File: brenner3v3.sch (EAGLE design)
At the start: 14 parts, among them IC1 REG1117, Q2 BC328, Q3 BC328

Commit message: Added PCB
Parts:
- R5: device rcl:R-EU_0207/10 -> rcl:R-EU_0207/2V
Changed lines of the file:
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@@
 <setting verticaltext="up"/>
 </settings>
-<grid distance="100" unitdist="mil" unit="mil" style="lines" multiple="1" display="yes" altdistance="100" altunitdist="mil" altunit="mil"/>
+<grid distance="0.1" unitdist="inch" unit="inch" style="lines" multiple="1" display="no" altdistance="0.01" altunitdist="inch" altunit="inch"/>
 <layers>
-<layer number="1" name="Top" color="4" fill="1" visible="no" active="no"/>
-<layer number="16" name="Bottom" color="1" fill="1" visible="no" active="no"/>
-<layer number="17" name="Pads" color="2" fill="1" visible="no" active="no"/>
-<layer number="18" name="Vias" color="2" fill="1" visible="no" active="no"/>
-<layer number="19" name="Unrouted" color="6" fill="1" visible="no" active="no"/>
-<layer number="20" name="Dimension" color="15" fill="1" visible="no" active="no"/>
-<layer number="21" name="tPlace" color="7" fill="1" visible="no" active="no"/>
-<layer number="22" name="bPlace" color="7" fill="1" visible="no" active="no"/>
-<layer number="23" name="tOrigins" color="15" fill="1" visible="no" active="no"/>
-<layer number="24" name="bOrigins" color="15" fill="1" visible="no" active="no"/>
-<layer number="25" name="tNames" color="7" fill="1" visible="no" active="no"/>
-<layer number="26" name="bNames" color="7" fill="1" visible="no" active="no"/>
-<layer number="27" name="tValues" color="7" fill="1" visible="no" active="no"/>
-<layer number="28" name="bValues" color="7" fill="1" visible="no" active="no"/>
+<layer number="1" name="Top" color="4" fill="1" visible="yes" active="no"/>
+<layer number="16" name="Bottom" color="1" fill="1" visible="yes" active="no"/>
+<layer number="17" name="Pads" color="2" fill="1" visible="yes" active="no"/>
+<layer number="18" name="Vias" color="2" fill="1" visible="yes" active="no"/>
+<layer number="19" name="Unrouted" color="6" fill="1" visible="yes" active="no"/>
+<layer number="20" name="Dimension" color="15" fill="1" visible="yes" active="no"/>
+<layer number="21" name="tPlace" color="7" fill="1" visible="yes" active="no"/>
+<layer number="22" name="bPlace" color="7" fill="1" visible="yes" active="no"/>
+<layer number="23" name="tOrigins" color="15" fill="1" visible="yes" active="no"/>
+<layer number="24" name="bOrigins" color="15" fill="1" visible="yes" active="no"/>
+<layer number="25" name="tNames" color="7" fill="1" visible="yes" active="no"/>
+<layer number="26" name="bNames" color="7" fill="1" visible="yes" active="no"/>
+<layer number="27" name="tValues" color="7" fill="1" visible="yes" active="no"/>
+<layer number="28" name="bValues" color="7" fill="1" visible="yes" active="no"/>
 <layer number="29" name="tStop" color="7" fill="3" visible="no" active="no"/>
 <layer number="30" name="bStop" color="7" fill="6" visible="no" active="no"/>
@@
 <layer number="35" name="tGlue" color="7" fill="4" visible="no" active="no"/>
 <layer number="36" name="bGlue" color="7" fill="5" visible="no" active="no"/>
-<layer number="37" name="tTest" color="7" fill="1" visible="no" active="no"/>
-<layer number="38" name="bTest" color="7" fill="1" visible="no" active="no"/>
+<layer number="37" name="tTest" color="7" fill="1" visible="yes" active="no"/>
+<layer number="38" name="bTest" color="7" fill="1" visible="yes" active="no"/>
 <layer number="39" name="tKeepout" color="4" fill="11" visible="no" active="no"/>
 <layer number="40" name="bKeepout" color="1" fill="11" visible="no" active="no"/>
@@
 <layer number="44" name="Drills" color="7" fill="1" visible="no" active="no"/>
 <layer number="45" name="Holes" color="7" fill="1" visible="no" active="no"/>
-<layer number="46" name="Milling" color="3" fill="1" visible="no" active="no"/>
-<layer number="47" name="Measures" color="7" fill="1" visible="no" active="no"/>
-<layer number="48" name="Document" color="7" fill="1" visible="no" active="no"/>
-<layer number="49" name="Reference" color="7" fill="1" visible="no" active="no"/>
-<layer number="51" name="tDocu" color="7" fill="1" visible="no" active="no"/>
-<layer number="52" name="bDocu" color="7" fill="1" visible="no" active="no"/>
+<layer number="46" name="Milling" color="3" fill="1" visible="yes" active="no"/>
+<layer number="47" name="Measures" color="7" fill="1" visible="yes" active="no"/>
+<layer number="48" name="Document" color="7" fill="1" visible="yes" active="no"/>
+<layer number="49" name="Reference" color="7" fill="1" visible="yes" active="no"/>
+<layer number="51" name="tDocu" color="7" fill="1" visible="yes" active="no"/>
+<layer number="52" name="bDocu" color="7" fill="1" visible="yes" active="no"/>
 <layer number="91" name="Nets" color="2" fill="1" visible="yes" active="yes"/>
 <layer number="92" name="Busses" color="1" fill="1" visible="yes" active="yes"/>
@@
 <part name="R3" library="rcl" deviceset="R-EU_" device="0207/10" value="10"/>
 <part name="R4" library="rcl" deviceset="R-EU_" device="0207/10" value="10"/>
-<part name="R5" library="rcl" deviceset="R-EU_" device="0207/10" value="820"/>
+<part name="R5" library="rcl" deviceset="R-EU_" device="0207/2V" value="820"/>
 <part name="D1" library="diode" deviceset="1N4004" device=""/>
 <part name="Q2" library="transistor" deviceset="*-PNP-" device="TO92-EBC" technology="BC328-25" value="BC328"/>

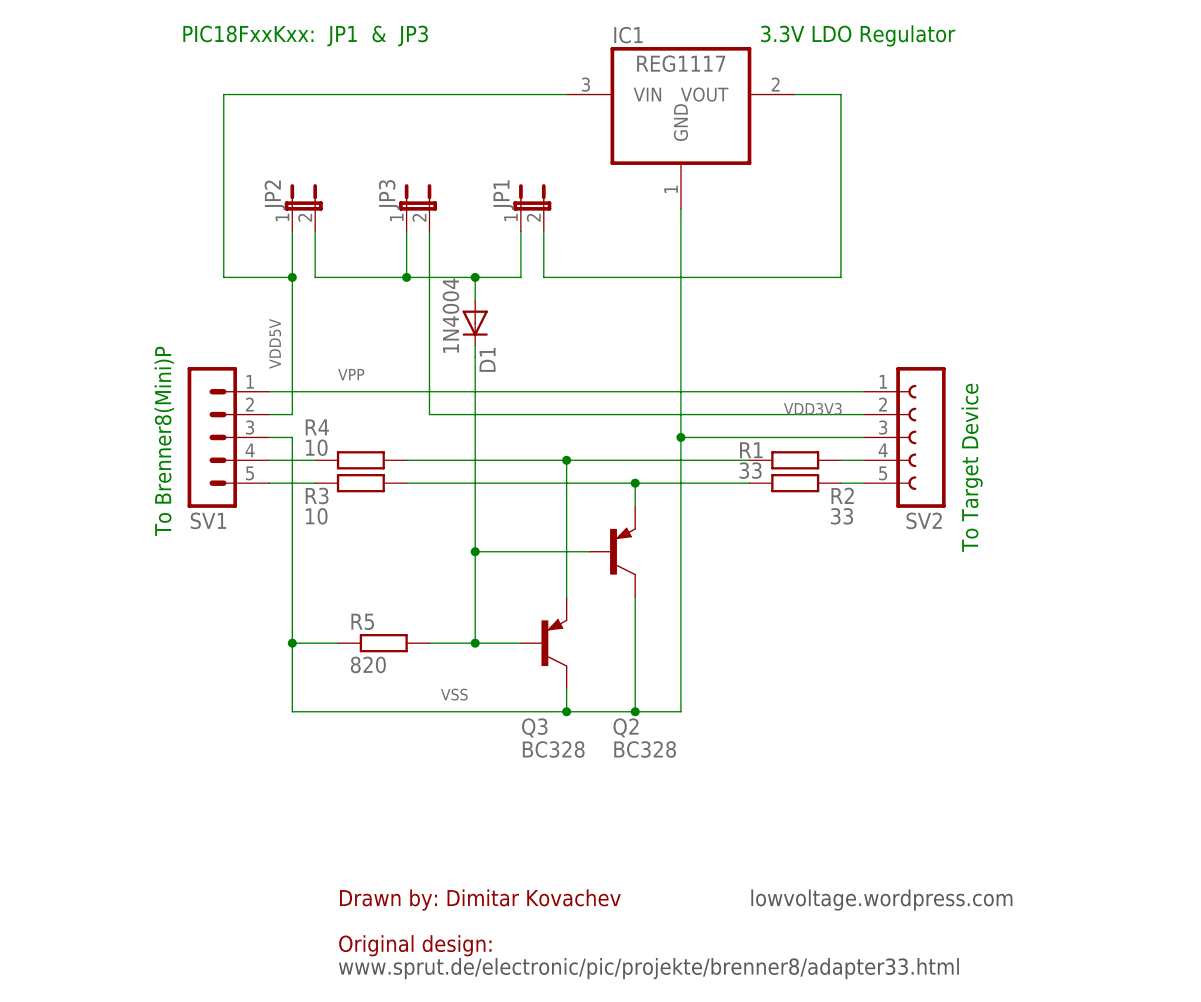
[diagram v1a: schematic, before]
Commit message: Simplified schematic & layout
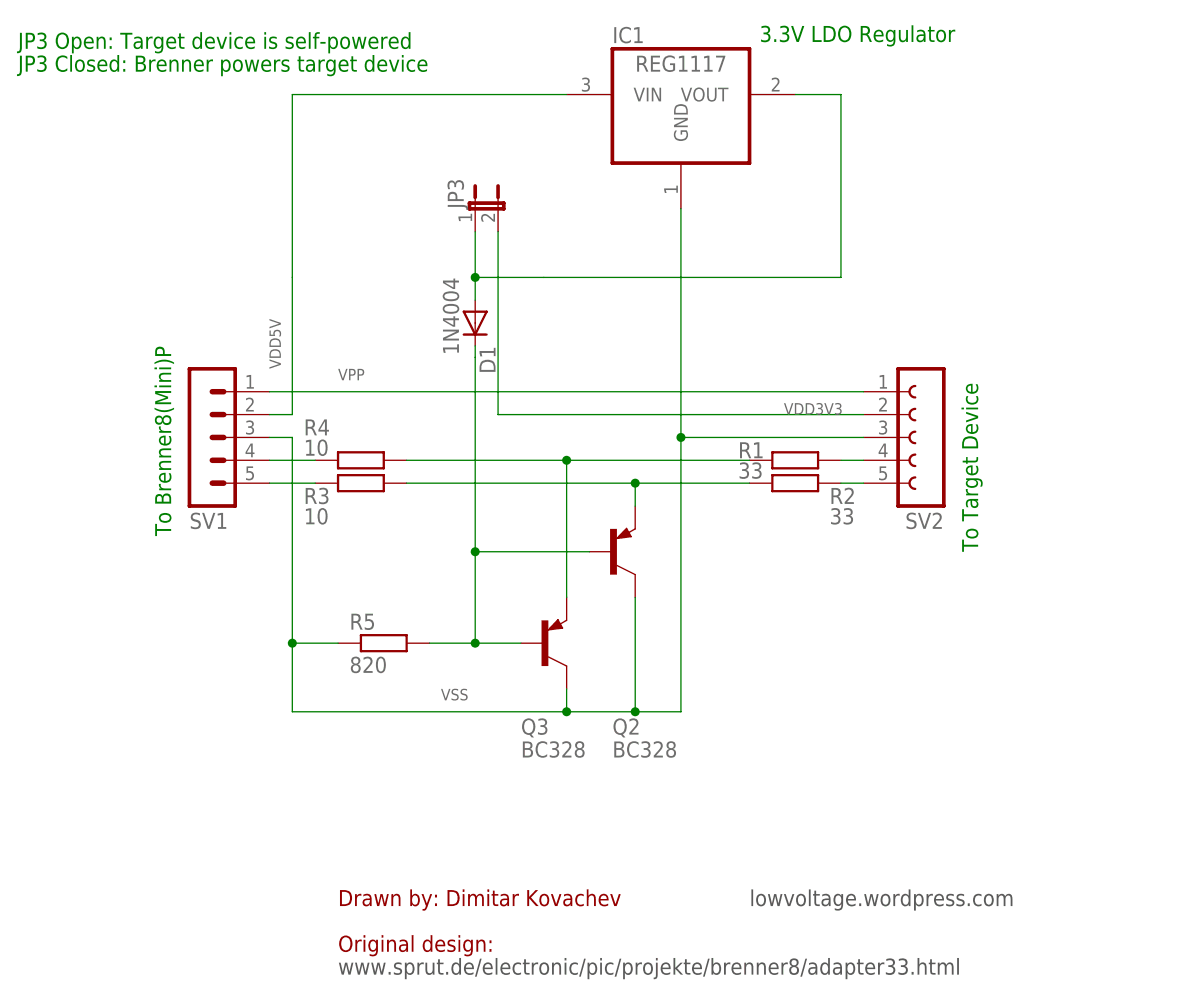
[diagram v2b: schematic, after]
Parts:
- removed JP1, JP2: (no value), jumper:JP1E
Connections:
- removed net N$1: IC1.VOUT, JP1.2
- net N$12: now also IC1.VOUT; no longer JP1.1, JP2.2
- net VDD5V: no longer JP2.1
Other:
- note added: "JP3 Closed: Brenner powers target device"
- note added: "JP3 Open: Target device is self-powered"
- note removed: "PIC18FxxKxx: JP1 & JP3"
- moved on the sheet: JP3
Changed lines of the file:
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@@
 <grid distance="0.1" unitdist="inch" unit="inch" style="lines" multiple="1" display="no" altdistance="0.01" altunitdist="inch" altunit="inch"/>
 <layers>
-<layer number="1" name="Top" color="4" fill="1" visible="yes" active="no"/>
-<layer number="16" name="Bottom" color="1" fill="1" visible="yes" active="no"/>
-<layer number="17" name="Pads" color="2" fill="1" visible="yes" active="no"/>
-<layer number="18" name="Vias" color="2" fill="1" visible="yes" active="no"/>
-<layer number="19" name="Unrouted" color="6" fill="1" visible="yes" active="no"/>
-<layer number="20" name="Dimension" color="15" fill="1" visible="yes" active="no"/>
-<layer number="21" name="tPlace" color="7" fill="1" visible="yes" active="no"/>
-<layer number="22" name="bPlace" color="7" fill="1" visible="yes" active="no"/>
-<layer number="23" name="tOrigins" color="15" fill="1" visible="yes" active="no"/>
-<layer number="24" name="bOrigins" color="15" fill="1" visible="yes" active="no"/>
-<layer number="25" name="tNames" color="7" fill="1" visible="yes" active="no"/>
-<layer number="26" name="bNames" color="7" fill="1" visible="yes" active="no"/>
-<layer number="27" name="tValues" color="7" fill="1" visible="yes" active="no"/>
-<layer number="28" name="bValues" color="7" fill="1" visible="yes" active="no"/>
+<layer number="1" name="Top" color="4" fill="1" visible="no" active="no"/>
+<layer number="16" name="Bottom" color="1" fill="1" visible="no" active="no"/>
+<layer number="17" name="Pads" color="2" fill="1" visible="no" active="no"/>
+<layer number="18" name="Vias" color="2" fill="1" visible="no" active="no"/>
+<layer number="19" name="Unrouted" color="6" fill="1" visible="no" active="no"/>
+<layer number="20" name="Dimension" color="15" fill="1" visible="no" active="no"/>
+<layer number="21" name="tPlace" color="7" fill="1" visible="no" active="no"/>
+<layer number="22" name="bPlace" color="7" fill="1" visible="no" active="no"/>
+<layer number="23" name="tOrigins" color="15" fill="1" visible="no" active="no"/>
+<layer number="24" name="bOrigins" color="15" fill="1" visible="no" active="no"/>
+<layer number="25" name="tNames" color="7" fill="1" visible="no" active="no"/>
+<layer number="26" name="bNames" color="7" fill="1" visible="no" active="no"/>
+<layer number="27" name="tValues" color="7" fill="1" visible="no" active="no"/>
+<layer number="28" name="bValues" color="7" fill="1" visible="no" active="no"/>
 <layer number="29" name="tStop" color="7" fill="3" visible="no" active="no"/>
 <layer number="30" name="bStop" color="7" fill="6" visible="no" active="no"/>
@@
 <layer number="35" name="tGlue" color="7" fill="4" visible="no" active="no"/>
 <layer number="36" name="bGlue" color="7" fill="5" visible="no" active="no"/>
-<layer number="37" name="tTest" color="7" fill="1" visible="yes" active="no"/>
-<layer number="38" name="bTest" color="7" fill="1" visible="yes" active="no"/>
+<layer number="37" name="tTest" color="7" fill="1" visible="no" active="no"/>
+<layer number="38" name="bTest" color="7" fill="1" visible="no" active="no"/>
 <layer number="39" name="tKeepout" color="4" fill="11" visible="no" active="no"/>
 <layer number="40" name="bKeepout" color="1" fill="11" visible="no" active="no"/>
@@
 <layer number="44" name="Drills" color="7" fill="1" visible="no" active="no"/>
 <layer number="45" name="Holes" color="7" fill="1" visible="no" active="no"/>
-<layer number="46" name="Milling" color="3" fill="1" visible="yes" active="no"/>
-<layer number="47" name="Measures" color="7" fill="1" visible="yes" active="no"/>
-<layer number="48" name="Document" color="7" fill="1" visible="yes" active="no"/>
-<layer number="49" name="Reference" color="7" fill="1" visible="yes" active="no"/>
-<layer number="51" name="tDocu" color="7" fill="1" visible="yes" active="no"/>
-<layer number="52" name="bDocu" color="7" fill="1" visible="yes" active="no"/>
+<layer number="46" name="Milling" color="3" fill="1" visible="no" active="no"/>
+<layer number="47" name="Measures" color="7" fill="1" visible="no" active="no"/>
+<layer number="48" name="Document" color="7" fill="1" visible="no" active="no"/>
+<layer number="49" name="Reference" color="7" fill="1" visible="no" active="no"/>
+<layer number="51" name="tDocu" color="7" fill="1" visible="no" active="no"/>
+<layer number="52" name="bDocu" color="7" fill="1" visible="no" active="no"/>
 <layer number="91" name="Nets" color="2" fill="1" visible="yes" active="yes"/>
 <layer number="92" name="Busses" color="1" fill="1" visible="yes" active="yes"/>
@@
 <part name="FRAME1" library="frames" deviceset="DINA4_P" device=""/>
 <part name="IC1" library="burr-brown" deviceset="REG1117" device=""/>
-<part name="JP1" library="jumper" deviceset="JP1E" device=""/>
-<part name="JP2" library="jumper" deviceset="JP1E" device=""/>
 <part name="JP3" library="jumper" deviceset="JP1E" device=""/>
 <part name="R1" library="rcl" deviceset="R-EU_" device="0207/10" value="33"/>
@@
 <text x="160.02" y="134.62" size="1.778" layer="91" rot="R180">3.3V LDO Regulator</text>
 <text x="71.12" y="99.06" size="1.778" layer="91" rot="R270">To Brenner8(Mini)P</text>
-<text x="101.6" y="134.62" size="1.778" layer="91" rot="R180">PIC18FxxKxx:  JP1  &amp;  JP3</text>
+<text x="55.88" y="132.08" size="1.778" layer="91">JP3 Open: Target device is self-powered</text>
+<text x="55.88" y="129.54" size="1.778" layer="91">JP3 Closed: Brenner powers target device</text>
 </plain>
 <instances>
@@
 <instance part="FRAME1" gate="G$2" x="88.9" y="5.08"/>
 <instance part="IC1" gate="G$1" x="129.54" y="127"/>
-<instance part="JP1" gate="A" x="111.76" y="114.3"/>
-<instance part="JP2" gate="A" x="86.36" y="114.3"/>
-<instance part="JP3" gate="A" x="99.06" y="114.3"/>
+<instance part="JP3" gate="A" x="106.68" y="114.3"/>
 <instance part="R1" gate="G$1" x="142.24" y="86.36" smashed="yes">
 <attribute name="NAME" x="135.89" y="86.5886" size="1.778" layer="95"/>
@@
 <segment>
 <pinref part="SV1" gate="G$1" pin="2"/>
-<pinref part="JP2" gate="A" pin="1"/>
 <wire x1="83.82" y1="91.44" x2="86.36" y2="91.44" width="0.1524" layer="91"/>
 <wire x1="86.36" y1="91.44" x2="86.36" y2="106.68" width="0.1524" layer="91"/>
-<wire x1="86.36" y1="106.68" x2="86.36" y2="111.76" width="0.1524" layer="91"/>
-<wire x1="86.36" y1="106.68" x2="78.74" y2="106.68" width="0.1524" layer="91"/>
-<wire x1="78.74" y1="106.68" x2="78.74" y2="127" width="0.1524" layer="91"/>
-<junction x="86.36" y="106.68"/>
+<wire x1="86.36" y1="106.68" x2="86.36" y2="127" width="0.1524" layer="91"/>
 <pinref part="IC1" gate="G$1" pin="VIN"/>
-<wire x1="78.74" y1="127" x2="116.84" y2="127" width="0.1524" layer="91"/>
+<wire x1="86.36" y1="127" x2="116.84" y2="127" width="0.1524" layer="91"/>
 <label x="85.09" y="96.52" size="1.27" layer="95" rot="R90"/>
 </segment>
 </net>
-<net name="N$1" class="0">
-<segment>
+<net name="N$12" class="0">
+<segment>
+<pinref part="JP3" gate="A" pin="1"/>
+<wire x1="106.68" y1="111.76" x2="106.68" y2="106.68" width="0.1524" layer="91"/>
+<pinref part="D1" gate="1" pin="A"/>
+<wire x1="106.68" y1="104.14" x2="106.68" y2="106.68" width="0.1524" layer="91"/>
+<junction x="106.68" y="106.68"/>
 <pinref part="IC1" gate="G$1" pin="VOUT"/>
 <wire x1="142.24" y1="127" x2="147.32" y2="127" width="0.1524" layer="91"/>
 <wire x1="147.32" y1="127" x2="147.32" y2="106.68" width="0.1524" layer="91"/>
 <wire x1="147.32" y1="106.68" x2="114.3" y2="106.68" width="0.1524" layer="91"/>
-<pinref part="JP1" gate="A" pin="2"/>
-<wire x1="114.3" y1="106.68" x2="114.3" y2="111.76" width="0.1524" layer="91"/>
-</segment>
-</net>
-<net name="N$12" class="0">
-<segment>
-<pinref part="JP2" gate="A" pin="2"/>
-<wire x1="88.9" y1="111.76" x2="88.9" y2="106.68" width="0.1524" layer="91"/>
-<wire x1="88.9" y1="106.68" x2="99.06" y2="106.68" width="0.1524" layer="91"/>
-<pinref part="JP1" gate="A" pin="1"/>
-<wire x1="99.06" y1="106.68" x2="106.68" y2="106.68" width="0.1524" layer="91"/>
-<wire x1="106.68" y1="106.68" x2="111.76" y2="106.68" width="0.1524" layer="91"/>
-<wire x1="111.76" y1="106.68" x2="111.76" y2="111.76" width="0.1524" layer="91"/>
-<pinref part="JP3" gate="A" pin="1"/>
-<wire x1="99.06" y1="111.76" x2="99.06" y2="106.68" width="0.1524" layer="91"/>
-<junction x="99.06" y="106.68"/>
-<pinref part="D1" gate="1" pin="A"/>
-<wire x1="106.68" y1="104.14" x2="106.68" y2="106.68" width="0.1524" layer="91"/>
-<junction x="106.68" y="106.68"/>
+<wire x1="106.68" y1="106.68" x2="114.3" y2="106.68" width="0.1524" layer="91"/>
 </segment>
 </net>
@@
 <segment>
 <pinref part="JP3" gate="A" pin="2"/>
-<wire x1="101.6" y1="111.76" x2="101.6" y2="91.44" width="0.1524" layer="91"/>
+<wire x1="109.22" y1="111.76" x2="109.22" y2="91.44" width="0.1524" layer="91"/>
 <pinref part="SV2" gate="G$1" pin="2"/>
-<wire x1="101.6" y1="91.44" x2="149.86" y2="91.44" width="0.1524" layer="91"/>
+<wire x1="109.22" y1="91.44" x2="149.86" y2="91.44" width="0.1524" layer="91"/>
 <label x="140.97" y="91.44" size="1.27" layer="95"/>
 </segment>
